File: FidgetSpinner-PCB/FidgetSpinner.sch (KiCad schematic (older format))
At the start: 37 parts, among them J1 EdgeConnector, Q1 Q_Photo_NPN, SW1 SW_POWER, SW2 button, U1 STM32L010K8T6

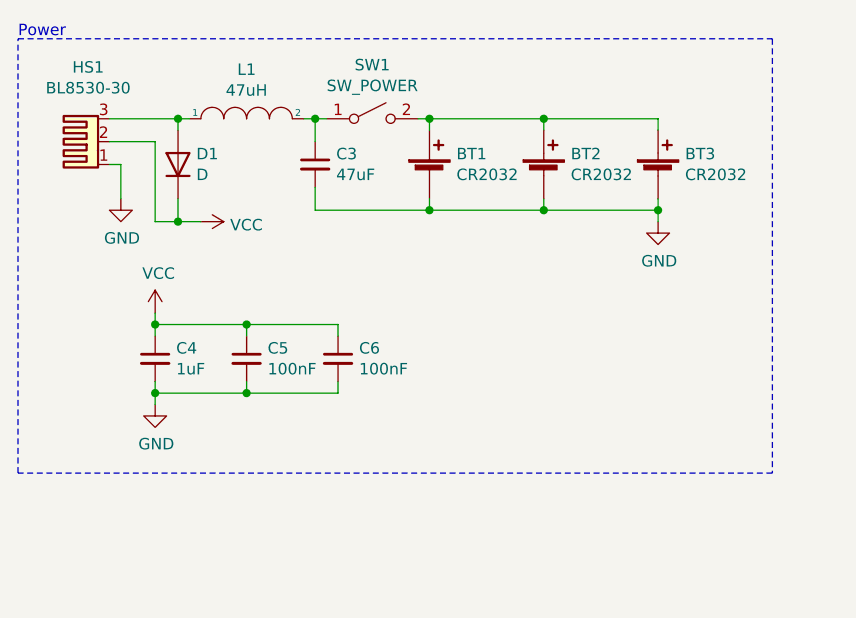
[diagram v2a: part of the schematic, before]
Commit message: button animations
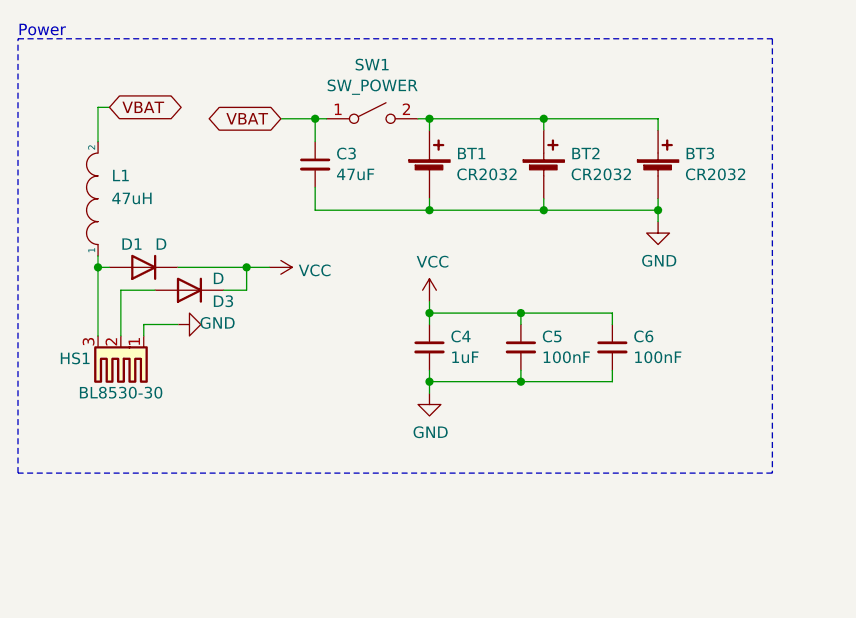
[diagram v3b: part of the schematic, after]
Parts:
- added D3: D, Diode_SMD:D_0805_2012Metric_Pad1.15x1.40mm_HandSolder, symbol Device:D
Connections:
- net VCC: now also D3.1 (K); no longer HS1.2
- net VBAT: now reaches C3.1, L1.2, SW1.1 (A)
- new net: D3.2 (A), HS1.2
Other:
- moved on the sheet: C4, C5, C6, D1, HS1, L1
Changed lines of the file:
@@
 L Mechanical:Heatsink_Pad_3Pin HS1
 U 1 1 612C4893
-P 2050 1500
-F 0 "HS1" V 2375 1493 50  0000 C CNN
-F 1 "BL8530-30" V 2284 1493 50  0000 C CNN
-F 2 "Package_TO_SOT_SMD:SOT-89-3_Handsoldering" H 2062 1450 50  0001 C CNN
-F 3 "~" H 2062 1450 50  0001 C CNN
-	1    2050 1500
-	0    -1   -1   0
+P 2200 2450
+F 0 "HS1" H 2400 2450 50  0000 C CNN
+F 1 "BL8530-30" H 2200 2600 50  0000 C CNN
+F 2 "Package_TO_SOT_SMD:SOT-89-3_Handsoldering" H 2212 2400 50  0001 C CNN
+F 3 "~" H 2212 2400 50  0001 C CNN
+	1    2200 2450
+	-1   0    0    1
 $EndComp
 $Comp
@@
 L power:VCC #PWR0102
 U 1 1 612C72CB
-P 2550 1850
-F 0 "#PWR0102" H 2550 1700 50  0001 C CNN
-F 1 "VCC" V 2565 1978 50  0000 L CNN
-F 2 "" H 2550 1850 50  0001 C CNN
-F 3 "" H 2550 1850 50  0001 C CNN
-	1    2550 1850
+P 2850 2050
+F 0 "#PWR0102" H 2850 1900 50  0001 C CNN
+F 1 "VCC" V 2865 2178 50  0000 L CNN
+F 2 "" H 2850 2050 50  0001 C CNN
+F 3 "" H 2850 2050 50  0001 C CNN
+	1    2850 2050
 	0    1    1    0
 $EndComp
@@
 L pspice:INDUCTOR L1
 U 1 1 612C88B1
-P 2750 1400
-F 0 "L1" H 2750 1615 50  0000 C CNN
-F 1 "47uH" H 2750 1524 50  0000 C CNN
-F 2 "Inductor_SMD:L_0805_2012Metric_Pad1.15x1.40mm_HandSolder" H 2750 1400 50  0001 C CNN
-F 3 "~" H 2750 1400 50  0001 C CNN
-	1    2750 1400
-	1    0    0    -1
+P 2100 1750
+F 0 "L1" V 2200 1650 50  0000 C CNN
+F 1 "47uH" V 2100 1600 50  0000 C CNN
+F 2 "Inductor_SMD:L_0805_2012Metric_Pad1.15x1.40mm_HandSolder" H 2100 1750 50  0001 C CNN
+F 3 "~" H 2100 1750 50  0001 C CNN
+	1    2100 1750
+	0    -1   -1   0
 $EndComp
 $Comp
@@
 L power:VCC #PWR0103
 U 1 1 612D1736
-P 2350 2250
-F 0 "#PWR0103" H 2350 2100 50  0001 C CNN
-F 1 "VCC" H 2365 2423 50  0000 C CNN
-F 2 "" H 2350 2250 50  0001 C CNN
-F 3 "" H 2350 2250 50  0001 C CNN
-	1    2350 2250
+P 3550 2200
+F 0 "#PWR0103" H 3550 2050 50  0001 C CNN
+F 1 "VCC" H 3565 2373 50  0000 C CNN
+F 2 "" H 3550 2200 50  0001 C CNN
+F 3 "" H 3550 2200 50  0001 C CNN
+	1    3550 2200
 	1    0    0    -1
 $EndComp
@@
 L power:GND #PWR0104
 U 1 1 612D1F2F
-P 2350 2650
-F 0 "#PWR0104" H 2350 2400 50  0001 C CNN
-F 1 "GND" H 2355 2477 50  0000 C CNN
-F 2 "" H 2350 2650 50  0001 C CNN
-F 3 "" H 2350 2650 50  0001 C CNN
-	1    2350 2650
+P 3550 2600
+F 0 "#PWR0104" H 3550 2350 50  0001 C CNN
+F 1 "GND" H 3555 2427 50  0000 C CNN
+F 2 "" H 3550 2600 50  0001 C CNN
+F 3 "" H 3550 2600 50  0001 C CNN
+	1    3550 2600
 	1    0    0    -1
 $EndComp
@@
 L Device:C_Small C4
 U 1 1 612D2237
-P 2350 2450
-F 0 "C4" H 2442 2496 50  0000 L CNN
-F 1 "1uF" H 2442 2405 50  0000 L CNN
-F 2 "Capacitor_SMD:C_0805_2012Metric_Pad1.18x1.45mm_HandSolder" H 2350 2450 50  0001 C CNN
-F 3 "~" H 2350 2450 50  0001 C CNN
-	1    2350 2450
+P 3550 2400
+F 0 "C4" H 3642 2446 50  0000 L CNN
+F 1 "1uF" H 3642 2355 50  0000 L CNN
+F 2 "Capacitor_SMD:C_0805_2012Metric_Pad1.18x1.45mm_HandSolder" H 3550 2400 50  0001 C CNN
+F 3 "~" H 3550 2400 50  0001 C CNN
+	1    3550 2400
 	1    0    0    -1
 $EndComp
@@
 L Device:C_Small C5
 U 1 1 612D2FA1
-P 2750 2450
-F 0 "C5" H 2842 2496 50  0000 L CNN
-F 1 "100nF" H 2842 2405 50  0000 L CNN
-F 2 "Capacitor_SMD:C_0805_2012Metric_Pad1.18x1.45mm_HandSolder" H 2750 2450 50  0001 C CNN
-F 3 "~" H 2750 2450 50  0001 C CNN
-	1    2750 2450
+P 3950 2400
+F 0 "C5" H 4042 2446 50  0000 L CNN
+F 1 "100nF" H 4042 2355 50  0000 L CNN
+F 2 "Capacitor_SMD:C_0805_2012Metric_Pad1.18x1.45mm_HandSolder" H 3950 2400 50  0001 C CNN
+F 3 "~" H 3950 2400 50  0001 C CNN
+	1    3950 2400
 	1    0    0    -1
 $EndComp
@@
 L Device:C_Small C6
 U 1 1 612D3376
-P 3150 2450
-F 0 "C6" H 3242 2496 50  0000 L CNN
-F 1 "100nF" H 3242 2405 50  0000 L CNN
-F 2 "Capacitor_SMD:C_0805_2012Metric_Pad1.18x1.45mm_HandSolder" H 3150 2450 50  0001 C CNN
-F 3 "~" H 3150 2450 50  0001 C CNN
-	1    3150 2450
-	1    0    0    -1
-$EndComp
-Wire Wire Line
-	2350 2250 2350 2300
-Wire Wire Line
-	2750 2350 2750 2300
-Wire Wire Line
-	2750 2300 2350 2300
-Connection ~ 2350 2300
-Wire Wire Line
-	2350 2300 2350 2350
-Wire Wire Line
-	3150 2350 3150 2300
-Wire Wire Line
-	3150 2300 2750 2300
-Connection ~ 2750 2300
-Wire Wire Line
-	2350 2550 2350 2600
-Wire Wire Line
-	2750 2550 2750 2600
-Wire Wire Line
-	2750 2600 2350 2600
-Connection ~ 2350 2600
-Wire Wire Line
-	2350 2600 2350 2650
-Wire Wire Line
-	3150 2550 3150 2600
-Wire Wire Line
-	3150 2600 2750 2600
-Connection ~ 2750 2600
+P 4350 2400
+F 0 "C6" H 4442 2446 50  0000 L CNN
+F 1 "100nF" H 4442 2355 50  0000 L CNN
+F 2 "Capacitor_SMD:C_0805_2012Metric_Pad1.18x1.45mm_HandSolder" H 4350 2400 50  0001 C CNN
+F 3 "~" H 4350 2400 50  0001 C CNN
+	1    4350 2400
+	1    0    0    -1
+$EndComp
+Wire Wire Line
+	3550 2200 3550 2250
+Wire Wire Line
+	3950 2300 3950 2250
+Wire Wire Line
+	3950 2250 3550 2250
+Connection ~ 3550 2250
+Wire Wire Line
+	3550 2250 3550 2300
+Wire Wire Line
+	4350 2300 4350 2250
+Wire Wire Line
+	4350 2250 3950 2250
+Connection ~ 3950 2250
+Wire Wire Line
+	3550 2500 3550 2550
+Wire Wire Line
+	3950 2500 3950 2550
+Wire Wire Line
+	3950 2550 3550 2550
+Connection ~ 3550 2550
+Wire Wire Line
+	3550 2550 3550 2600
+Wire Wire Line
+	4350 2500 4350 2550
+Wire Wire Line
+	4350 2550 3950 2550
+Connection ~ 3950 2550
 $Comp
 L Device:Battery_Cell BT2
@@
 L power:GND #PWR0105
 U 1 1 612E12E2
-P 2200 1750
-F 0 "#PWR0105" H 2200 1500 50  0001 C CNN
-F 1 "GND" H 2205 1577 50  0000 C CNN
-F 2 "" H 2200 1750 50  0001 C CNN
-F 3 "" H 2200 1750 50  0001 C CNN
-	1    2200 1750
-	1    0    0    -1
-$EndComp
-Wire Wire Line
-	2150 1600 2200 1600
-Wire Wire Line
-	2200 1600 2200 1750
+P 2450 2300
+F 0 "#PWR0105" H 2450 2050 50  0001 C CNN
+F 1 "GND" V 2455 2127 50  0000 C CNN
+F 2 "" H 2450 2300 50  0001 C CNN
+F 3 "" H 2450 2300 50  0001 C CNN
+	1    2450 2300
+	0    -1   -1   0
+$EndComp
+Wire Wire Line
+	2300 2350 2300 2300
+Wire Wire Line
+	2300 2300 2450 2300
 $Comp
 L Device:D D1
 U 1 1 612E43C6
-P 2450 1600
-F 0 "D1" V 2496 1520 50  0000 R CNN
-F 1 "D" V 2405 1520 50  0000 R CNN
-F 2 "Diode_SMD:D_0805_2012Metric_Pad1.15x1.40mm_HandSolder" H 2450 1600 50  0001 C CNN
-F 3 "~" H 2450 1600 50  0001 C CNN
-	1    2450 1600
-	0    -1   -1   0
+P 2300 2050
+F 0 "D1" H 2400 1950 50  0000 R CNN
+F 1 "D" H 2250 1950 50  0000 R CNN
+F 2 "Diode_SMD:D_0805_2012Metric_Pad1.15x1.40mm_HandSolder" H 2300 2050 50  0001 C CNN
+F 3 "~" H 2300 2050 50  0001 C CNN
+	1    2300 2050
+	-1   0    0    1
 $EndComp
 Wire Wire Line
 	4550 1850 4550 1800
 Connection ~ 4550 1800
-Wire Wire Line
-	3000 1400 3050 1400
 Connection ~ 3050 1400
 Wire Wire Line
-	2150 1400 2450 1400
-Wire Wire Line
-	2450 1450 2450 1400
-Connection ~ 2450 1400
-Wire Wire Line
-	2450 1400 2500 1400
-Wire Wire Line
-	2150 1500 2350 1500
-Wire Wire Line
-	2350 1500 2350 1850
-Wire Wire Line
-	2350 1850 2450 1850
-Wire Wire Line
-	2450 1750 2450 1850
-Connection ~ 2450 1850
-Wire Wire Line
-	2450 1850 2550 1850
+	2100 2350 2100 2050
+Wire Wire Line
+	2150 2050 2100 2050
+Connection ~ 2100 2050
+Wire Wire Line
+	2100 2050 2100 2000
+Wire Wire Line
+	2200 2350 2200 2150
 $Comp
 L power:GND #PWR0106
@@
 NoConn ~ 3900 4350
 NoConn ~ 3900 4250
+Text GLabel 2900 1400 0    50   BiDi ~ 0
+VBAT
+$Comp
+L Device:D D3
+U 1 1 6137F251
+P 2500 2150
+F 0 "D3" H 2400 2200 50  0000 R CNN
+F 1 "D" H 2400 2100 50  0000 R CNN
+F 2 "Diode_SMD:D_0805_2012Metric_Pad1.15x1.40mm_HandSolder" H 2500 2150 50  0001 C CNN
+F 3 "~" H 2500 2150 50  0001 C CNN
+	1    2500 2150
+	-1   0    0    1
+$EndComp
+Wire Wire Line
+	2200 2150 2350 2150
+Wire Wire Line
+	2450 2050 2750 2050
+Wire Wire Line
+	2650 2150 2750 2150
+Wire Wire Line
+	2750 2150 2750 2050
+Connection ~ 2750 2050
+Wire Wire Line
+	2750 2050 2850 2050
+Text GLabel 2150 1350 2    50   BiDi ~ 0
+VBAT
+Wire Wire Line
+	2150 1350 2100 1350
+Wire Wire Line
+	2100 1350 2100 1500
+Wire Wire Line
+	2900 1400 3050 1400
 $EndSCHEMATC

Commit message: backup of CLion project
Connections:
- net GND: no longer R1.1, R2.1, R3.1, R4.1, R5.1, R6.1, R7.1, R8.1
- net VCC: now also R1.1, R2.1, R3.1, R4.1, R5.1, R6.1, R7.1, R8.1
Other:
- moved on the sheet: D10, D11, D12, D13, D14, D15, D16, D17, R1, R2, R3, R4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

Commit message: updated
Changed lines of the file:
@@
 	9550 1400 9550 1300
 Connection ~ 9550 1400
+Text GLabel 2500 4250 0    50   BiDi ~ 0
+VBAT
 $EndSCHEMATC

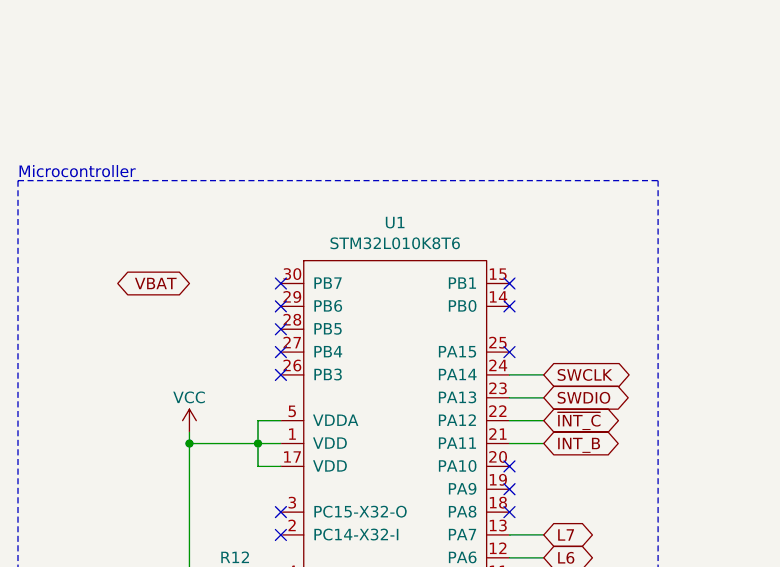
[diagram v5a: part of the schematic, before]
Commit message: added battery to ADC connection for PCB
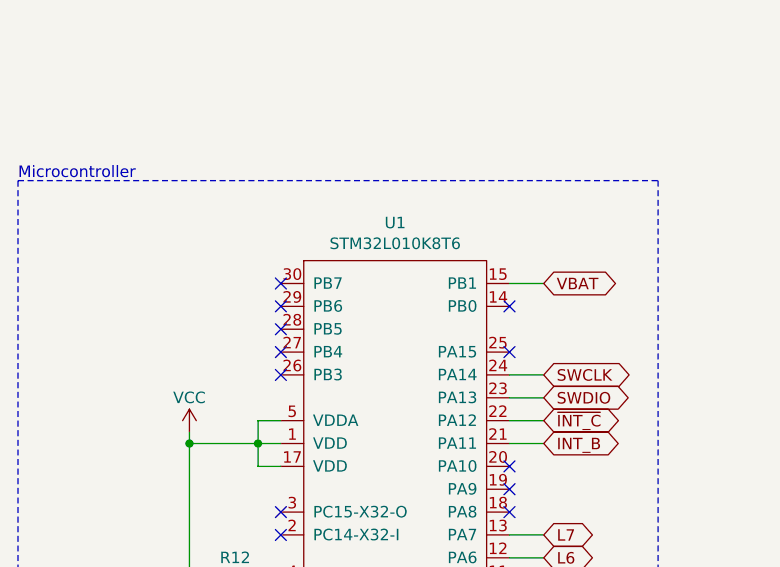
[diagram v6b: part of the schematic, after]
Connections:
- net VBAT: now also U1.15 (PB1)
- no-connect marks 13 -> 12
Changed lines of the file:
@@
 NoConn ~ 3900 4550
 NoConn ~ 3900 4350
-NoConn ~ 3900 4250
 Text GLabel 2900 1400 0    50   BiDi ~ 0
 VBAT
@@
 	9550 1400 9550 1300
 Connection ~ 9550 1400
-Text GLabel 2500 4250 0    50   BiDi ~ 0
+Text GLabel 4050 4250 2    50   BiDi ~ 0
 VBAT
+Wire Wire Line
+	3900 4250 4050 4250
 $EndSCHEMATC

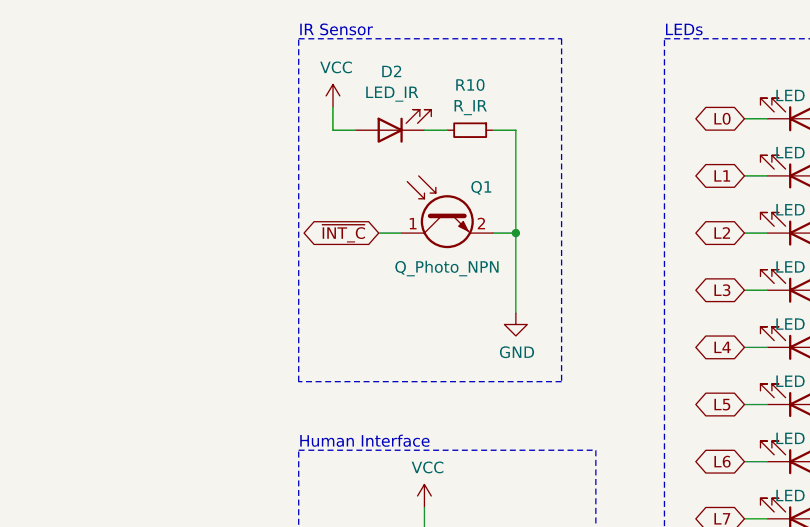
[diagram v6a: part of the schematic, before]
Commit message: using GP2S27 optic sensor
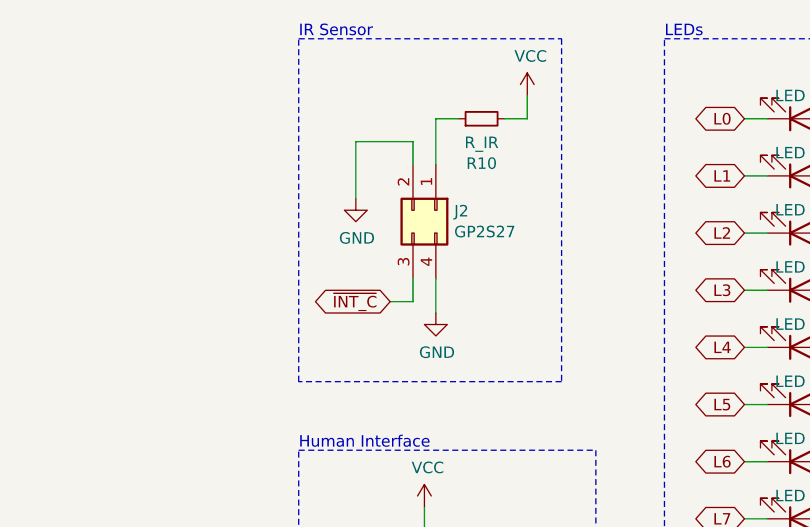
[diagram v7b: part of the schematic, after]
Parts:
- removed D2: LED_IR, Diode_SMD:D_0805_2012Metric_Pad1.15x1.40mm_HandSolder, symbol Device:LED
- removed Q1: Q_Photo_NPN, Diode_SMD:D_0805_2012Metric_Pad1.15x1.40mm_HandSolder, symbol Device:Q_Photo_NPN
- added J2: GP2S27, WYW_Package:4pin_5040, symbol Connector_Generic:Conn_02x02_Counter_Clockwise
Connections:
- net GND: now also J2.2 (Pin_2), J2.4 (Pin_4); no longer R10.1
- net VCC: now also R10.2
- net ~INT_C: now also J2.3 (Pin_3)
- new net: J2.1 (Pin_1), R10.1
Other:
- moved on the sheet: R10
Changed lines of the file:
@@
 INT_B
-$Comp
-L Device:LED D2
-U 1 1 613466D1
-P 7200 1450
-F 0 "D2" H 7193 1195 50  0000 C CNN
-F 1 "LED_IR" H 7193 1286 50  0000 C CNN
-F 2 "Diode_SMD:D_0805_2012Metric_Pad1.15x1.40mm_HandSolder" H 7200 1450 50  0001 C CNN
-F 3 "~" H 7200 1450 50  0001 C CNN
-	1    7200 1450
-	-1   0    0    1
-$EndComp
 $Comp
 L Switch:SW_Push SW2
@@
 L power:VCC #PWR05
 U 1 1 6136EBD5
-P 6950 1350
-F 0 "#PWR05" H 6950 1200 50  0001 C CNN
-F 1 "VCC" H 6965 1523 50  0000 C CNN
-F 2 "" H 6950 1350 50  0001 C CNN
-F 3 "" H 6950 1350 50  0001 C CNN
-	1    6950 1350
+P 7800 1300
+F 0 "#PWR05" H 7800 1150 50  0001 C CNN
+F 1 "VCC" H 7815 1473 50  0000 C CNN
+F 2 "" H 7800 1300 50  0001 C CNN
+F 3 "" H 7800 1300 50  0001 C CNN
+	1    7800 1300
 	1    0    0    -1
 $EndComp
@@
 L Device:R_Small R10
 U 1 1 61370063
-P 7550 1450
-F 0 "R10" V 7354 1450 50  0000 C CNN
-F 1 "R_IR" V 7445 1450 50  0000 C CNN
-F 2 "Resistor_SMD:R_0805_2012Metric_Pad1.20x1.40mm_HandSolder" H 7550 1450 50  0001 C CNN
-F 3 "~" H 7550 1450 50  0001 C CNN
-	1    7550 1450
-	0    1    1    0
-$EndComp
-$Comp
-L power:GND #PWR06
-U 1 1 6137064F
-P 7750 2250
-F 0 "#PWR06" H 7750 2000 50  0001 C CNN
-F 1 "GND" H 7755 2077 50  0000 C CNN
-F 2 "" H 7750 2250 50  0001 C CNN
-F 3 "" H 7750 2250 50  0001 C CNN
-	1    7750 2250
-	1    0    0    -1
-$EndComp
-Wire Wire Line
-	6950 1350 6950 1450
-Wire Wire Line
-	6950 1450 7050 1450
-Wire Wire Line
-	7350 1450 7450 1450
-Wire Wire Line
-	7650 1450 7750 1450
-Text GLabel 7150 1900 0    50   BiDi ~ 0
+P 7600 1400
+F 0 "R10" V 7404 1400 50  0000 C CNN
+F 1 "R_IR" V 7495 1400 50  0000 C CNN
+F 2 "Resistor_SMD:R_0805_2012Metric_Pad1.20x1.40mm_HandSolder" H 7600 1400 50  0001 C CNN
+F 3 "~" H 7600 1400 50  0001 C CNN
+	1    7600 1400
+	0    -1   -1   0
+$EndComp
+Text GLabel 7200 2200 0    50   BiDi ~ 0
 ~INT_C
 Wire Wire Line
@@
 Microcontroller
 $Comp
-L Device:Q_Photo_NPN Q1
-U 1 1 6163779A
-P 7450 1800
-F 0 "Q1" V 7350 1650 50  0000 C CNN
-F 1 "Q_Photo_NPN" V 7700 1800 50  0000 C CNN
-F 2 "Diode_SMD:D_0805_2012Metric_Pad1.15x1.40mm_HandSolder" H 7650 1900 50  0001 C CNN
-F 3 "~" H 7450 1800 50  0001 C CNN
-	1    7450 1800
-	0    -1   1    0
-$EndComp
-Wire Wire Line
-	7750 1450 7750 1900
-Wire Wire Line
-	7650 1900 7750 1900
-Connection ~ 7750 1900
-Wire Wire Line
-	7150 1900 7250 1900
-Wire Wire Line
-	7750 1900 7750 2250
-$Comp
 L Device:R_Small R9
 U 1 1 61682058
@@
 	2900 1400 3050 1400
 $Comp
-L power:VCC #PWR?
+L power:VCC #PWR0108
 U 1 1 6140C001
 P 9550 1300
-F 0 "#PWR?" H 9550 1150 50  0001 C CNN
+F 0 "#PWR0108" H 9550 1150 50  0001 C CNN
 F 1 "VCC" H 9550 1450 50  0000 C CNN
 F 2 "" H 9550 1300 50  0001 C CNN
@@
 Wire Wire Line
 	3900 4250 4050 4250
+$Comp
+L Connector_Generic:Conn_02x02_Counter_Clockwise J2
+U 1 1 6148767D
+P 7400 1800
+F 0 "J2" V 7404 1880 50  0000 L CNN
+F 1 "GP2S27" V 7495 1880 50  0000 L CNN
+F 2 "WYW_Package:4pin_5040" H 7400 1800 50  0001 C CNN
+F 3 "~" H 7400 1800 50  0001 C CNN
+	1    7400 1800
+	0    1    1    0
+$EndComp
+$Comp
+L power:GND #PWR?
+U 1 1 614AAA47
+P 7050 1750
+F 0 "#PWR?" H 7050 1500 50  0001 C CNN
+F 1 "GND" H 7055 1577 50  0000 C CNN
+F 2 "" H 7050 1750 50  0001 C CNN
+F 3 "" H 7050 1750 50  0001 C CNN
+	1    7050 1750
+	1    0    0    -1
+$EndComp
+$Comp
+L power:GND #PWR?
+U 1 1 614AB14B
+P 7400 2250
+F 0 "#PWR?" H 7400 2000 50  0001 C CNN
+F 1 "GND" H 7405 2077 50  0000 C CNN
+F 2 "" H 7400 2250 50  0001 C CNN
+F 3 "" H 7400 2250 50  0001 C CNN
+	1    7400 2250
+	1    0    0    -1
+$EndComp
+Wire Wire Line
+	7050 1750 7050 1500
+Wire Wire Line
+	7050 1500 7300 1500
+Wire Wire Line
+	7300 1500 7300 1600
+Wire Wire Line
+	7400 1600 7400 1400
+Wire Wire Line
+	7400 1400 7500 1400
+Wire Wire Line
+	7700 1400 7800 1400
+Wire Wire Line
+	7800 1400 7800 1300
+Wire Wire Line
+	7300 2100 7300 2200
+Wire Wire Line
+	7300 2200 7200 2200
+Wire Wire Line
+	7400 2100 7400 2250
 $EndSCHEMATC

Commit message: important updates
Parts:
- BT1, BT2, BT3: value CR2032 -> CR2450; footprint WYW_Package:CR2450_Centered -> Battery:BatteryHolder_Keystone_3009_1x2450
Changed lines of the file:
@@
 P 3550 1650
 F 0 "BT1" H 3668 1746 50  0000 L CNN
-F 1 "CR2032" H 3668 1655 50  0000 L CNN
-F 2 "WYW_Package:CR2450_Centered" V 3550 1710 50  0001 C CNN
+F 1 "CR2450" H 3668 1655 50  0000 L CNN
+F 2 "Battery:BatteryHolder_Keystone_3009_1x2450" V 3550 1710 50  0001 C CNN
 F 3 "~" V 3550 1710 50  0001 C CNN
 	1    3550 1650
@@
 P 4050 1650
 F 0 "BT2" H 4168 1746 50  0000 L CNN
-F 1 "CR2032" H 4168 1655 50  0000 L CNN
-F 2 "WYW_Package:CR2450_Centered" V 4050 1710 50  0001 C CNN
+F 1 "CR2450" H 4168 1655 50  0000 L CNN
+F 2 "Battery:BatteryHolder_Keystone_3009_1x2450" V 4050 1710 50  0001 C CNN
 F 3 "~" V 4050 1710 50  0001 C CNN
 	1    4050 1650
@@
 P 4550 1650
 F 0 "BT3" H 4668 1746 50  0000 L CNN
-F 1 "CR2032" H 4668 1655 50  0000 L CNN
-F 2 "WYW_Package:CR2450_Centered" V 4550 1710 50  0001 C CNN
+F 1 "CR2450" H 4668 1655 50  0000 L CNN
+F 2 "Battery:BatteryHolder_Keystone_3009_1x2450" V 4550 1710 50  0001 C CNN
 F 3 "~" V 4550 1710 50  0001 C CNN
 	1    4550 1650
@@
 $EndComp
 $Comp
-L power:GND #PWR?
+L power:GND #PWR0109
 U 1 1 614AAA47
 P 7050 1750
-F 0 "#PWR?" H 7050 1500 50  0001 C CNN
+F 0 "#PWR0109" H 7050 1500 50  0001 C CNN
 F 1 "GND" H 7055 1577 50  0000 C CNN
 F 2 "" H 7050 1750 50  0001 C CNN
@@
 $EndComp
 $Comp
-L power:GND #PWR?
+L power:GND #PWR0110
 U 1 1 614AB14B
 P 7400 2250
-F 0 "#PWR?" H 7400 2000 50  0001 C CNN
+F 0 "#PWR0110" H 7400 2000 50  0001 C CNN
 F 1 "GND" H 7405 2077 50  0000 C CNN
 F 2 "" H 7400 2250 50  0001 C CNN
